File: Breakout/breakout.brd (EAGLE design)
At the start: 52.6 x 42.5 mm, 49 parts, among them Q1 16Mhz, U1 TPS63001DRCT, U11 XL

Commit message: via added
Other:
- board text removed: "GND"
- board text removed: "RX"
- board text removed: "SOP2"
- board text removed: "VCC"
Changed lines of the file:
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@@
 <?xml version="1.0" encoding="utf-8"?>
 <!DOCTYPE eagle SYSTEM "eagle.dtd">
-<eagle version="7.2.0">
+<eagle version="7.1.0">
 <drawing>
 <settings>
@@
 <dimension x1="12.93" y1="-113.03" x2="13.94" y2="-110.52" x3="7.63" y3="-111.775" textsize="1.778" layer="37" dtype="vertical"/>
 <dimension x1="13.95" y1="-21.57" x2="11.43" y2="-21.83" x3="12.69" y3="-4.13" textsize="1.778" layer="37" dtype="horizontal"/>
-<text x="54.1528" y="5.6388" size="1.27" layer="25" font="vector" ratio="18" rot="R90">GND</text>
-<text x="51.6128" y="5.6388" size="1.27" layer="25" font="vector" ratio="18" rot="R90">VCC</text>
-<text x="48.9966" y="5.5372" size="1.016" layer="25" font="vector" ratio="18" rot="R90">SOP2</text>
-<text x="46.5328" y="6.6548" size="1.27" layer="25" font="vector" ratio="18" rot="R90">RX</text>
 </plain>
 <attributes>
@@
 <via x="43.608" y="22.9916" extent="1-16" drill="0.6"/>
 <contactref element="R24" pad="2"/>
-<wire x1="24.5" y1="1.4" x2="56.49" y2="1.4" width="0" layer="19" extent="1-1"/>
-<wire x1="23.8" y1="1.8" x2="24.5" y2="1.4" width="0" layer="19" extent="1-1"/>
-<wire x1="23.8" y1="2.8" x2="23.8" y2="1.8" width="0" layer="19" extent="1-1"/>
-<wire x1="23.8" y1="3.8" x2="23.8" y2="2.8" width="0" layer="19" extent="1-1"/>
-<wire x1="23.8" y1="4.8" x2="23.8" y2="3.8" width="0" layer="19" extent="1-1"/>
-<wire x1="23.8" y1="5.8" x2="23.8" y2="4.8" width="0" layer="19" extent="1-1"/>
-<wire x1="24.5" y1="6.3" x2="23.8" y2="5.8" width="0" layer="19" extent="1-1"/>
-<wire x1="21.1434" y1="5.1386" x2="23.8" y2="4.8" width="0" layer="19" extent="1-1"/>
-<wire x1="21.0134" y1="2.9086" x2="21.1434" y2="5.1386" width="0" layer="19" extent="1-1"/>
-<wire x1="27.3" y1="6.3" x2="24.5" y2="6.3" width="0" layer="19" extent="1-1"/>
-<wire x1="28.3" y1="6.3" x2="27.3" y2="6.3" width="0" layer="19" extent="1-1"/>
-<wire x1="29.3" y1="6.3" x2="28.3" y2="6.3" width="0" layer="19" extent="1-1"/>
-<wire x1="30.3" y1="6.3" x2="29.3" y2="6.3" width="0" layer="19" extent="1-1"/>
-<wire x1="31.3" y1="5.8" x2="30.3" y2="6.3" width="0" layer="19" extent="1-1"/>
-<wire x1="31.3" y1="4.8" x2="31.3" y2="5.8" width="0" layer="19" extent="1-1"/>
-<wire x1="31.3" y1="3.8" x2="31.3" y2="4.8" width="0" layer="19" extent="1-1"/>
-<wire x1="31.3" y1="2.8" x2="31.3" y2="3.8" width="0" layer="19" extent="1-1"/>
-<wire x1="27.15" y1="7.6" x2="27.3" y2="6.3" width="0" layer="19" extent="1-1"/>
-<wire x1="30.65" y1="1.4" x2="31.3" y2="2.8" width="0" layer="19" extent="1-1"/>
-<wire x1="27" y1="9.35" x2="27.15" y2="7.6" width="0" layer="19" extent="1-1"/>
-<wire x1="27" y1="10.55" x2="27" y2="9.35" width="0" layer="19" extent="1-1"/>
-<wire x1="27" y1="11.7" x2="27" y2="10.55" width="0" layer="19" extent="1-1"/>
-<wire x1="24.75" y1="10.5" x2="27" y2="10.55" width="0" layer="19" extent="1-1"/>
-<wire x1="24.75" y1="11.7" x2="24.75" y2="10.5" width="0" layer="19" extent="1-1"/>
-<wire x1="24.75" y1="9.3" x2="24.75" y2="10.5" width="0" layer="19" extent="1-1"/>
-<wire x1="32.508" y1="7.9216" x2="31.3" y2="5.8" width="0" layer="19" extent="1-1"/>
-<wire x1="34.728" y1="7.9616" x2="32.508" y2="7.9216" width="0" layer="19" extent="1-1"/>
-<wire x1="34.798" y1="10.2616" x2="34.728" y2="7.9616" width="0" layer="19" extent="1-1"/>
-<wire x1="32.578" y1="10.2216" x2="34.798" y2="10.2616" width="0" layer="19" extent="1-1"/>
-<wire x1="27.155" y1="14.27" x2="27" y2="11.7" width="0" layer="19" extent="1-1"/>
-<wire x1="24.615" y1="14.27" x2="27.155" y2="14.27" width="0" layer="19" extent="1-1"/>
-<wire x1="22.075" y1="14.27" x2="24.615" y2="14.27" width="0" layer="19" extent="1-1"/>
-<wire x1="22.075" y1="15.94" x2="22.075" y2="14.27" width="0" layer="19" extent="1-1"/>
-<wire x1="34.8234" y1="5.3086" x2="34.728" y2="7.9616" width="0" layer="19" extent="1-1"/>
-<wire x1="34.8534" y1="2.9486" x2="34.8234" y2="5.3086" width="0" layer="19" extent="1-1"/>
-<wire x1="21.1034" y1="8.1086" x2="21.1434" y2="5.1386" width="0" layer="19" extent="1-1"/>
+<via x="48.7334" y="37.5586" extent="1-16" drill="0.6"/>
+<via x="51.0534" y="37.5586" extent="1-16" drill="0.6"/>
+<wire x1="38.35" y1="38.064" x2="37.842" y2="39.5372" width="0" layer="19" extent="1-1"/>
+<wire x1="38.35" y1="36.5908" x2="38.35" y2="38.064" width="0" layer="19" extent="1-1"/>
+<wire x1="41.586" y1="37.366" x2="38.35" y2="38.064" width="0" layer="19" extent="1-1"/>
+<wire x1="49.2928" y1="4.19" x2="48.84" y2="7.12" width="0" layer="19" extent="1-1"/>
+<wire x1="22.07" y1="30.315" x2="23.5" y2="33.54" width="0" layer="19" extent="1-16"/>
+<wire x1="37.748" y1="33.0042" x2="38.35" y2="36.5908" width="0" layer="19" extent="1-1"/>
+<wire x1="39.85" y1="30.315" x2="37.748" y2="33.0042" width="0" layer="19" extent="1-1"/>
 <wire x1="34.775" y1="14.27" x2="34.798" y2="10.2616" width="0" layer="19" extent="1-1"/>
-<wire x1="39.15" y1="5.62" x2="34.8234" y2="5.3086" width="0" layer="19" extent="1-1"/>
-<wire x1="39.16" y1="7.22" x2="39.15" y2="5.62" width="0" layer="19" extent="1-1"/>
-<wire x1="40.27" y1="3.75" x2="39.15" y2="5.62" width="0" layer="19" extent="1-1"/>
-<wire x1="43.34" y1="9.12" x2="39.16" y2="7.22" width="0" layer="19" extent="1-1"/>
-<wire x1="43.34" y1="10.12" x2="43.34" y2="9.12" width="0" layer="19" extent="1-1"/>
-<wire x1="41.125" y1="14.27" x2="43.34" y2="10.12" width="0" layer="19" extent="1-1"/>
-<wire x1="45.84" y1="15.62" x2="41.125" y2="14.27" width="0" layer="19" extent="1-1"/>
-<wire x1="50.34" y1="15.62" x2="45.84" y2="15.62" width="0" layer="19" extent="1-1"/>
-<wire x1="50.72" y1="18.48" x2="50.34" y2="15.62" width="0" layer="19" extent="1-1"/>
-<wire x1="54.426" y1="19.918" x2="50.72" y2="18.48" width="0" layer="19" extent="1-1"/>
-<wire x1="49.23" y1="22.37" x2="50.72" y2="18.48" width="0" layer="19" extent="1-1"/>
-<wire x1="51.84" y1="11.12" x2="50.34" y2="15.62" width="0" layer="19" extent="1-1"/>
-<wire x1="55.9" y1="9.03" x2="51.84" y2="11.12" width="0" layer="19" extent="1-1"/>
-<wire x1="48.84" y1="7.12" x2="51.84" y2="11.12" width="0" layer="19" extent="1-1"/>
-<wire x1="49.2928" y1="4.19" x2="48.84" y2="7.12" width="0" layer="19" extent="1-1"/>
-<wire x1="43.608" y1="22.9916" x2="49.23" y2="22.37" width="0" layer="19" extent="1-1"/>
-<wire x1="36.1" y1="20.79" x2="34.775" y2="14.27" width="0" layer="19" extent="1-1"/>
-<wire x1="36.1" y1="23.79" x2="36.1" y2="20.79" width="0" layer="19" extent="1-1"/>
-<wire x1="35.85" y1="26.54" x2="36.1" y2="23.79" width="0" layer="19" extent="1-1"/>
-<wire x1="33.1" y1="26.79" x2="35.85" y2="26.54" width="0" layer="19" extent="1-1"/>
-<wire x1="33.1" y1="23.79" x2="36.1" y2="23.79" width="0" layer="19" extent="1-1"/>
-<wire x1="33.1" y1="20.79" x2="36.1" y2="20.79" width="0" layer="19" extent="1-1"/>
-<wire x1="30.1" y1="26.79" x2="33.1" y2="26.79" width="0" layer="19" extent="1-1"/>
-<wire x1="30.1" y1="23.79" x2="33.1" y2="23.79" width="0" layer="19" extent="1-1"/>
-<wire x1="30.1" y1="20.79" x2="33.1" y2="20.79" width="0" layer="19" extent="1-1"/>
-<wire x1="39.85" y1="30.315" x2="35.85" y2="26.54" width="0" layer="19" extent="1-1"/>
-<wire x1="41.12" y1="30.315" x2="39.85" y2="30.315" width="0" layer="19" extent="1-1"/>
-<wire x1="37.748" y1="33.0042" x2="39.85" y2="30.315" width="0" layer="19" extent="1-1"/>
-<wire x1="38.35" y1="36.5908" x2="37.748" y2="33.0042" width="0" layer="19" extent="1-1"/>
-<wire x1="38.35" y1="38.064" x2="38.35" y2="36.5908" width="0" layer="19" extent="1-1"/>
-<wire x1="37.842" y1="39.5372" x2="38.35" y2="38.064" width="0" layer="19" extent="1-1"/>
-<wire x1="41.586" y1="37.366" x2="38.35" y2="36.5908" width="0" layer="19" extent="1-1"/>
-<wire x1="41.76" y1="35.19" x2="41.586" y2="37.366" width="0" layer="19" extent="1-1"/>
-<wire x1="56.5912" y1="4.7264" x2="55.9" y2="9.03" width="0" layer="19" extent="1-1"/>
-<wire x1="27.32" y1="35.09" x2="30.1" y2="26.79" width="0" layer="19" extent="1-1"/>
+<wire x1="21.84" y1="37.19" x2="23.5" y2="33.54" width="0" layer="19" extent="1-16"/>
+<wire x1="27.32" y1="35.09" x2="23.5" y2="33.54" width="0" layer="19" extent="1-16"/>
 <wire x1="29.285" y1="36.09" x2="27.32" y2="35.09" width="0" layer="19" extent="1-1"/>
 <wire x1="28.32" y1="37.055" x2="29.285" y2="36.09" width="0" layer="19" extent="1-1"/>
-<wire x1="23.5" y1="33.54" x2="27.32" y2="35.09" width="0" layer="19" extent="1-16"/>
-<wire x1="22.07" y1="30.315" x2="23.5" y2="33.54" width="0" layer="19" extent="1-16"/>
-<wire x1="21.84" y1="37.19" x2="23.5" y2="33.54" width="0" layer="19" extent="1-16"/>
-<wire x1="21.87" y1="39.77" x2="21.84" y2="37.19" width="0" layer="19" extent="1-1"/>
-<wire x1="17.81" y1="34.2" x2="21.84" y2="37.19" width="0" layer="19" extent="1-1"/>
-<wire x1="13.248" y1="34.8016" x2="17.81" y2="34.2" width="0" layer="19" extent="1-1"/>
-<wire x1="17.94" y1="25.39" x2="22.07" y2="30.315" width="0" layer="19" extent="1-1"/>
-<wire x1="61.12" y1="27.93" x2="54.426" y2="19.918" width="0" layer="19" extent="1-1"/>
-<wire x1="58.39" y1="32.79" x2="61.12" y2="27.93" width="0" layer="19" extent="1-1"/>
+<wire x1="39.15" y1="5.62" x2="34.8234" y2="5.3086" width="0" layer="19" extent="1-1"/>
+<wire x1="45.84" y1="15.62" x2="50.34" y2="15.62" width="0" layer="19" extent="1-1"/>
+<wire x1="17.81" y1="34.2" x2="13.248" y2="34.8016" width="0" layer="19" extent="1-1"/>
+<wire x1="43.34" y1="9.12" x2="39.16" y2="7.22" width="0" layer="19" extent="1-1"/>
+<wire x1="41.125" y1="14.27" x2="43.34" y2="10.12" width="0" layer="19" extent="1-1"/>
 </signal>
 <signal name="N$1">

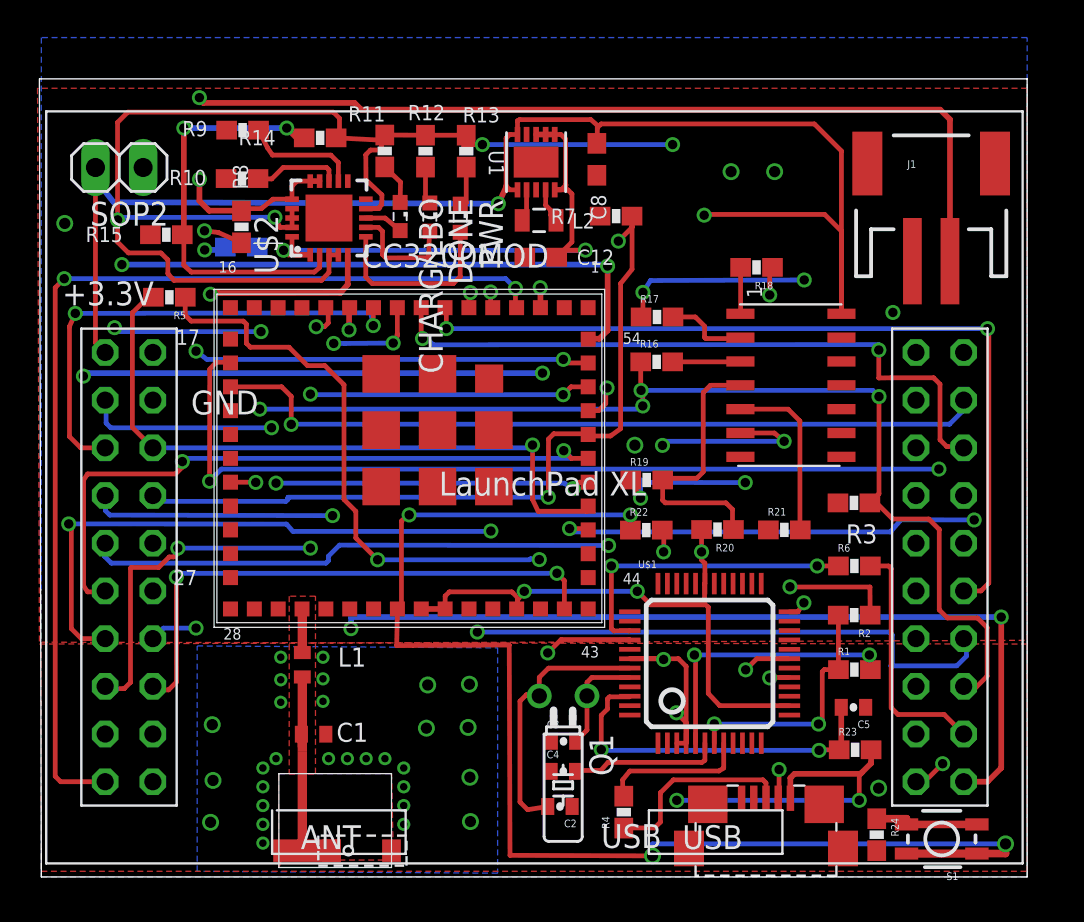
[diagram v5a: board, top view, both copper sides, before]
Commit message: Fix some un-routed ground
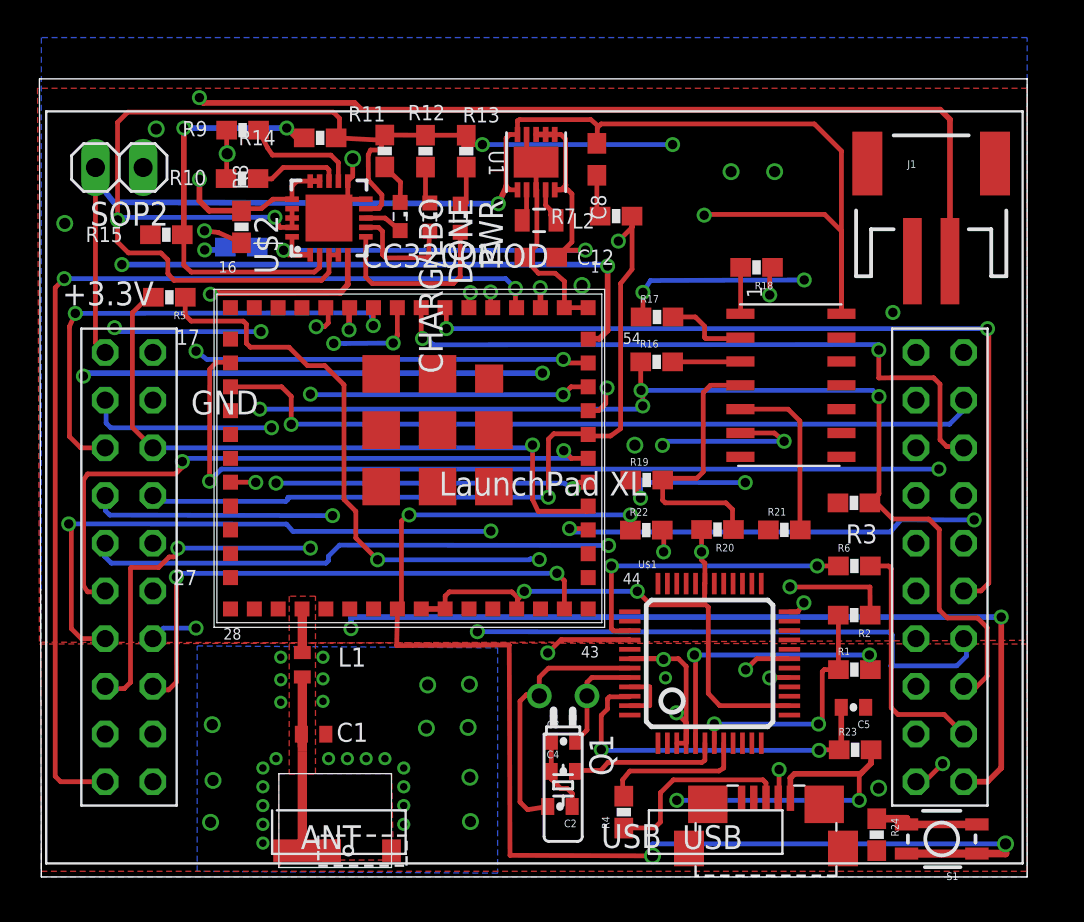
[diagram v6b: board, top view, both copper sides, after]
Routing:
- net GND: track 0.00 -> 32.1 mm, vias 34 -> 39

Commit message: more ground fixed
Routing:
- net GND: track 32.1 -> 36.9 mm, vias 39 -> 42
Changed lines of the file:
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@@
 <wire x1="40.28" y1="4.44" x2="40.28" y2="3.76" width="0.254" layer="1"/>
 <wire x1="40.28" y1="3.76" x2="40.27" y2="3.75" width="0.254" layer="1"/>
-<wire x1="58.39" y1="32.79" x2="61.12" y2="27.93" width="0" layer="19" extent="1-1"/>
-<wire x1="51.0534" y1="37.5586" x2="58.39" y2="32.79" width="0" layer="19" extent="1-1"/>
-<wire x1="48.7334" y1="37.5586" x2="51.0534" y2="37.5586" width="0" layer="19" extent="1-1"/>
-<wire x1="41.586" y1="37.366" x2="48.7334" y2="37.5586" width="0" layer="19" extent="1-1"/>
-<wire x1="38.39" y1="36.5908" x2="41.586" y2="37.366" width="0" layer="19" extent="1-1"/>
-<wire x1="40.7934" y1="31.4986" x2="39.86" y2="31.72" width="0" layer="19" extent="1-1"/>
-<wire x1="35.85" y1="26.54" x2="39.85" y2="30.315" width="0" layer="19" extent="1-1"/>
-<wire x1="36.1" y1="23.79" x2="35.85" y2="26.54" width="0" layer="19" extent="1-1"/>
-<wire x1="33.1" y1="26.79" x2="35.85" y2="26.54" width="0" layer="19" extent="1-1"/>
-<wire x1="33.1" y1="23.79" x2="36.1" y2="23.79" width="0" layer="19" extent="1-1"/>
-<wire x1="36.1" y1="20.79" x2="36.1" y2="23.79" width="0" layer="19" extent="1-1"/>
-<wire x1="33.1" y1="20.79" x2="33.1" y2="23.79" width="0" layer="19" extent="1-1"/>
-<wire x1="30.1" y1="26.79" x2="33.1" y2="26.79" width="0" layer="19" extent="1-1"/>
-<wire x1="30.1" y1="23.79" x2="33.1" y2="23.79" width="0" layer="19" extent="1-1"/>
-<wire x1="30.1" y1="20.79" x2="33.1" y2="20.79" width="0" layer="19" extent="1-1"/>
-<wire x1="34.775" y1="14.27" x2="36.1" y2="20.79" width="0" layer="19" extent="1-1"/>
-<wire x1="34.798" y1="10.2616" x2="34.775" y2="14.27" width="0" layer="19" extent="1-1"/>
-<wire x1="32.578" y1="10.2216" x2="34.798" y2="10.2616" width="0" layer="19" extent="1-1"/>
-<wire x1="34.728" y1="7.9616" x2="34.798" y2="10.2616" width="0" layer="19" extent="1-1"/>
-<wire x1="32.508" y1="7.9216" x2="34.728" y2="7.9616" width="0" layer="19" extent="1-1"/>
-<wire x1="31.3" y1="5.8" x2="32.508" y2="7.9216" width="0" layer="19" extent="1-1"/>
-<wire x1="31.3" y1="4.8" x2="31.3" y2="5.8" width="0" layer="19" extent="1-1"/>
-<wire x1="31.3" y1="3.8" x2="31.3" y2="4.8" width="0" layer="19" extent="1-1"/>
-<wire x1="31.3" y1="2.8" x2="31.3" y2="3.8" width="0" layer="19" extent="1-1"/>
-<wire x1="30.3" y1="6.3" x2="31.3" y2="5.8" width="0" layer="19" extent="1-1"/>
-<wire x1="29.3" y1="6.3" x2="30.3" y2="6.3" width="0" layer="19" extent="1-1"/>
-<wire x1="28.3" y1="6.3" x2="29.3" y2="6.3" width="0" layer="19" extent="1-1"/>
-<wire x1="27.3" y1="6.3" x2="28.3" y2="6.3" width="0" layer="19" extent="1-1"/>
-<wire x1="27.15" y1="7.6" x2="27.3" y2="6.3" width="0" layer="19" extent="1-1"/>
-<wire x1="30.65" y1="1.4" x2="31.3" y2="2.8" width="0" layer="19" extent="1-1"/>
-<wire x1="27" y1="9.35" x2="27.15" y2="7.6" width="0" layer="19" extent="1-1"/>
-<wire x1="27" y1="10.55" x2="27" y2="9.35" width="0" layer="19" extent="1-1"/>
-<wire x1="27" y1="11.7" x2="27" y2="10.55" width="0" layer="19" extent="1-1"/>
-<wire x1="24.75" y1="10.5" x2="27" y2="10.55" width="0" layer="19" extent="1-1"/>
-<wire x1="24.75" y1="11.7" x2="24.75" y2="10.5" width="0" layer="19" extent="1-1"/>
-<wire x1="24.75" y1="9.3" x2="24.75" y2="10.5" width="0" layer="19" extent="1-1"/>
-<wire x1="27.155" y1="14.27" x2="27" y2="11.7" width="0" layer="19" extent="1-1"/>
-<wire x1="24.615" y1="14.27" x2="27.155" y2="14.27" width="0" layer="19" extent="1-1"/>
-<wire x1="22.075" y1="14.27" x2="24.615" y2="14.27" width="0" layer="19" extent="1-1"/>
-<wire x1="22.075" y1="15.94" x2="22.075" y2="14.27" width="0" layer="19" extent="1-1"/>
-<wire x1="34.8234" y1="5.3086" x2="34.728" y2="7.9616" width="0" layer="19" extent="1-1"/>
-<wire x1="34.8534" y1="2.9486" x2="34.8234" y2="5.3086" width="0" layer="19" extent="1-1"/>
-<wire x1="24.5" y1="6.3" x2="27.3" y2="6.3" width="0" layer="19" extent="1-1"/>
-<wire x1="23.8" y1="5.8" x2="24.5" y2="6.3" width="0" layer="19" extent="1-1"/>
-<wire x1="23.8" y1="4.8" x2="23.8" y2="5.8" width="0" layer="19" extent="1-1"/>
-<wire x1="23.8" y1="3.8" x2="23.8" y2="4.8" width="0" layer="19" extent="1-1"/>
-<wire x1="23.8" y1="2.8" x2="23.8" y2="3.8" width="0" layer="19" extent="1-1"/>
-<wire x1="23.8" y1="1.8" x2="23.8" y2="2.8" width="0" layer="19" extent="1-1"/>
-<wire x1="24.5" y1="1.4" x2="23.8" y2="1.8" width="0" layer="19" extent="1-1"/>
-<wire x1="21.1434" y1="5.1386" x2="23.8" y2="4.8" width="0" layer="19" extent="1-1"/>
-<wire x1="21.0134" y1="2.9086" x2="21.1434" y2="5.1386" width="0" layer="19" extent="1-1"/>
-<wire x1="21.1034" y1="8.1086" x2="21.1434" y2="5.1386" width="0" layer="19" extent="1-1"/>
-<wire x1="39.15" y1="5.62" x2="34.8234" y2="5.3086" width="0" layer="19" extent="1-1"/>
-<wire x1="43.34" y1="9.12" x2="39.16" y2="7.22" width="0" layer="19" extent="1-1"/>
-<wire x1="45.24" y1="10.6" x2="44.4" y2="10.12" width="0" layer="19" extent="1-1"/>
-<wire x1="41.125" y1="14.27" x2="43.34" y2="10.12" width="0" layer="19" extent="1-1"/>
-<wire x1="48.84" y1="7.12" x2="44.4" y2="9.12" width="0" layer="19" extent="1-1"/>
-<wire x1="49.2928" y1="4.19" x2="48.84" y2="7.12" width="0" layer="19" extent="1-1"/>
-<wire x1="45.84" y1="15.62" x2="41.125" y2="14.27" width="0" layer="19" extent="1-1"/>
+<wire x1="22.075" y1="15.94" x2="22.075" y2="14.27" width="0.4064" layer="1"/>
+<via x="33.82" y="13.09" extent="1-16" drill="0.4"/>
+<wire x1="34.775" y1="14.27" x2="34.61" y2="14.27" width="0.4064" layer="1"/>
+<wire x1="34.61" y1="14.27" x2="34.61" y2="13.29" width="0.4064" layer="1"/>
+<wire x1="34.61" y1="13.29" x2="33.82" y2="13.29" width="0.4064" layer="1"/>
+<wire x1="33.82" y1="13.29" x2="33.82" y2="13.09" width="0.4064" layer="1"/>
+<via x="38.61" y="2.28" extent="1-16" drill="0.4"/>
+<via x="49.16" y="3.16" extent="1-16" drill="0.4"/>
 <wire x1="50.34" y1="15.62" x2="45.84" y2="15.62" width="0" layer="19" extent="1-1"/>
-<wire x1="50.72" y1="18.48" x2="50.34" y2="15.62" width="0" layer="19" extent="1-1"/>
-<wire x1="54.426" y1="19.918" x2="50.72" y2="18.48" width="0" layer="19" extent="1-1"/>
-<wire x1="49.23" y1="22.37" x2="50.72" y2="18.48" width="0" layer="19" extent="1-1"/>
-<wire x1="51.84" y1="11.12" x2="50.34" y2="15.62" width="0" layer="19" extent="1-1"/>
-<wire x1="55.9" y1="9.03" x2="51.84" y2="11.12" width="0" layer="19" extent="1-1"/>
-<wire x1="56.5912" y1="4.7264" x2="55.9" y2="9.03" width="0" layer="19" extent="1-1"/>
-<wire x1="56.49" y1="1.4" x2="56.5912" y2="4.7264" width="0" layer="19" extent="1-1"/>
-<wire x1="43.608" y1="22.9916" x2="49.23" y2="22.37" width="0" layer="19" extent="1-1"/>
-<wire x1="27.32" y1="35.09" x2="30.1" y2="26.79" width="0" layer="19" extent="1-1"/>
-<wire x1="23.5" y1="33.54" x2="27.32" y2="35.09" width="0" layer="19" extent="1-16"/>
 <wire x1="22.07" y1="30.315" x2="23.5" y2="33.54" width="0" layer="19" extent="1-16"/>
-<wire x1="21.84" y1="37.19" x2="23.5" y2="33.54" width="0" layer="19" extent="1-16"/>
-<wire x1="21.898" y1="38.5116" x2="21.87" y2="39.77" width="0" layer="19" extent="1-1"/>
-<wire x1="18.118" y1="39.8316" x2="21.87" y2="39.77" width="0" layer="19" extent="1-1"/>
-<wire x1="17.81" y1="34.2" x2="21.84" y2="37.19" width="0" layer="19" extent="1-1"/>
-<wire x1="13.248" y1="34.8016" x2="17.81" y2="34.2" width="0" layer="19" extent="1-1"/>
-<wire x1="17.94" y1="25.39" x2="22.07" y2="30.315" width="0" layer="19" extent="1-1"/>
+<wire x1="49.2928" y1="4.19" x2="49.2928" y2="3.2928" width="0.254" layer="1"/>
+<wire x1="49.2928" y1="3.2928" x2="49.16" y2="3.16" width="0.254" layer="1"/>
 </signal>
 <signal name="N$1">
@@
 <via x="34.85" y="31.12" extent="1-16" drill="0.5"/>
 <wire x1="34.85" y1="31.12" x2="34.86" y2="13.4" width="0.254" layer="15"/>
-<wire x1="34.86" y1="13.4" x2="35.22" y2="13.06" width="0.254" layer="15"/>
-<via x="35.22" y="13.06" extent="1-16" drill="0.5"/>
-<wire x1="35.22" y1="13.06" x2="57.16" y2="13.04" width="0.254" layer="16"/>
+<wire x1="34.86" y1="13.4" x2="35.44" y2="13.07" width="0.254" layer="15"/>
+<via x="35.44" y="13.07" extent="1-16" drill="0.5"/>
+<wire x1="35.44" y1="13.07" x2="57.16" y2="13.04" width="0.254" layer="16"/>
 <wire x1="57.16" y1="13.04" x2="57.32" y2="12.88" width="0.254" layer="16"/>
 <wire x1="57.32" y1="12.88" x2="57.32" y2="11.32" width="0.254" layer="16"/>
@@
 <contactref element="CC3200MOD" pad="P42"/>
 <contactref element="U11" pad="GPIO_30"/>
-<wire x1="39.855" y1="14.27" x2="39.855" y2="15.775" width="0.254" layer="1"/>
-<wire x1="39.855" y1="15.775" x2="39.46" y2="16.17" width="0.254" layer="1"/>
 <via x="39.46" y="16.17" extent="1-16" drill="0.5"/>
 <wire x1="39.46" y1="16.17" x2="19.23" y2="16.17" width="0.254" layer="16"/>
@@
 <wire x1="18.78" y1="9.96" x2="18.13" y2="9.96" width="0.254" layer="1"/>
 <wire x1="18.13" y1="9.96" x2="17.94" y2="10.15" width="0.254" layer="1"/>
+<wire x1="39.46" y1="16.17" x2="39.46" y2="14.665" width="0.254" layer="1"/>
+<wire x1="39.46" y1="14.665" x2="39.855" y2="14.27" width="0.254" layer="1"/>
 </signal>
 <signal name="N$15">
